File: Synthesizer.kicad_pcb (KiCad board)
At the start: 6 copper layers, 169 parts, among them J1 USB_A, J2 AudioJack3, J3 USB_B_Micro, J4 FPGA_debug, J5 MCU_debug, J6 67997-410HLF, SW1 SW_Push, SW10 SW_Push, SW11 SW_Push, SW12 SW_Push, SW13 SW_Push, SW14 SW_Push, SW15 SW_Push, SW16 SW_Push, SW2 SW_Push, SW3 SW_Push, SW4 SW_Push, SW5 SW_Push, SW6 SW_Push, SW7 SW_Push, SW8 SW_Push, SW9 SW_Push, U1 TPD3S014, U2 S25FL127S, U3 XC7A100T-FTG256, U4 Oscillator, U5 TPS54325, U6 TPS54294, U7 EFM32GG11B4xx, U8 PCM5102, Y1 48Mhz

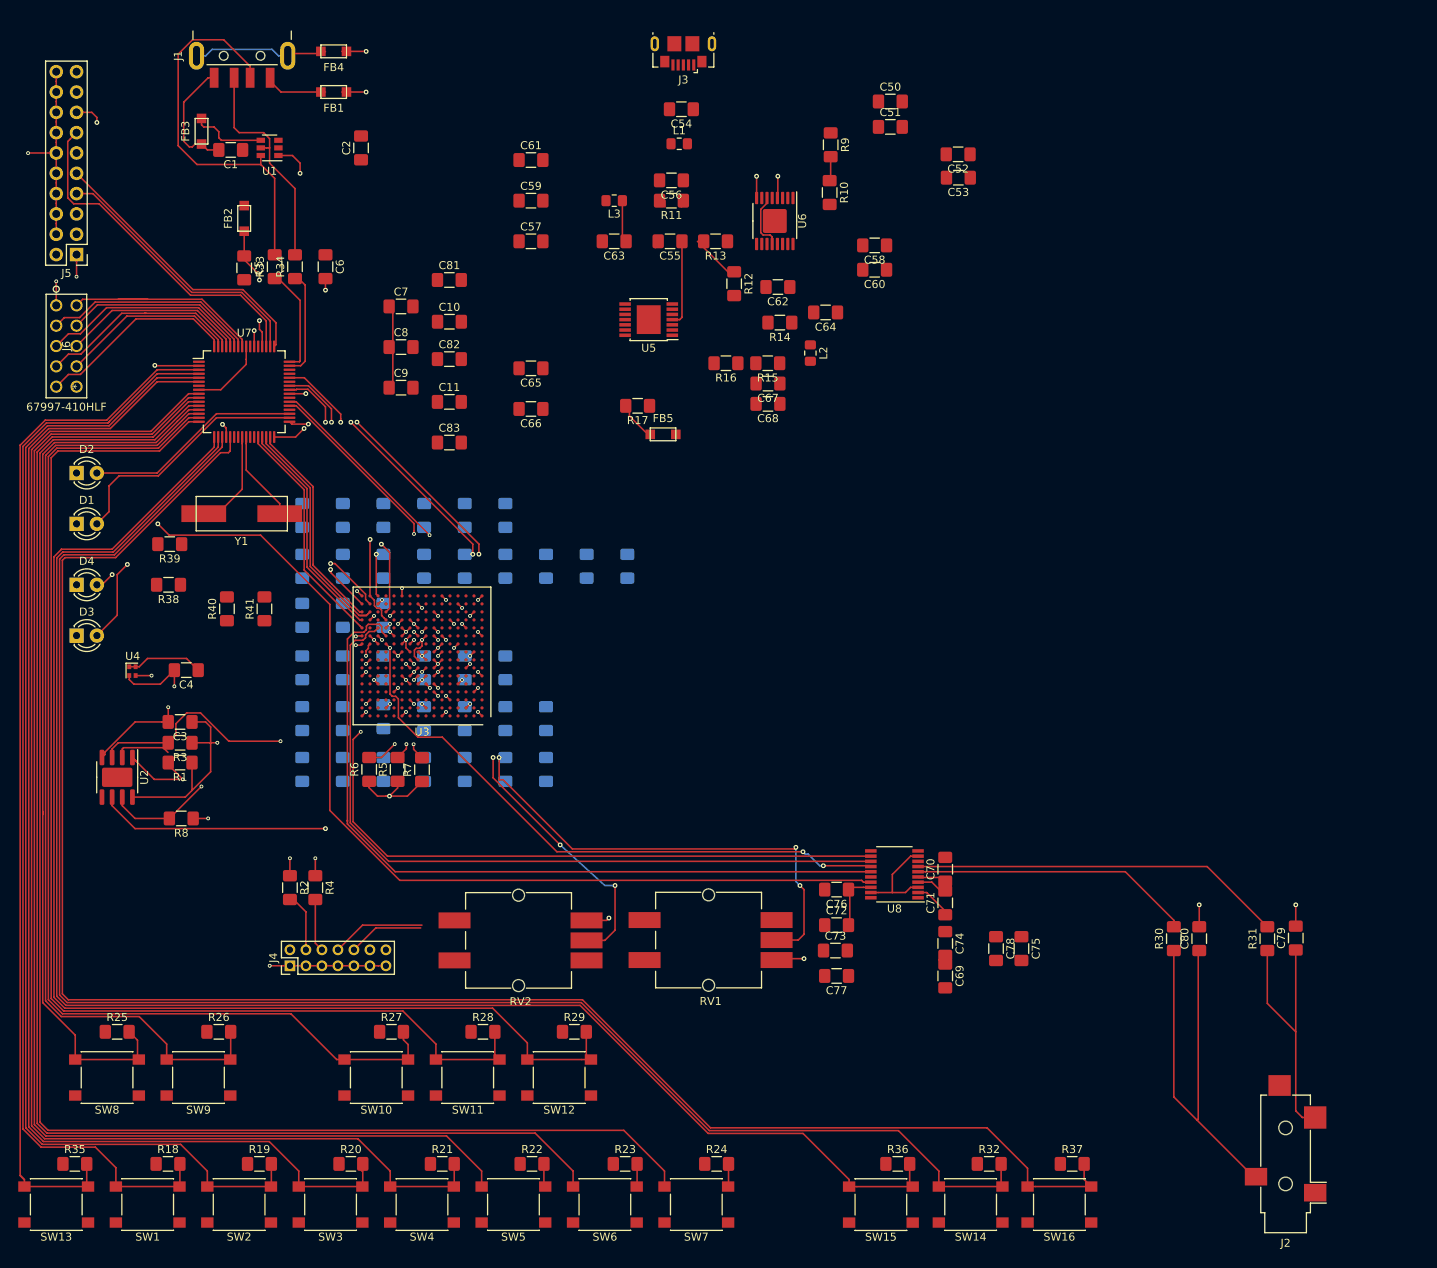
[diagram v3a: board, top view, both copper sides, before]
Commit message: Wire up 1V PSU. Use smaller footprints for small caps.
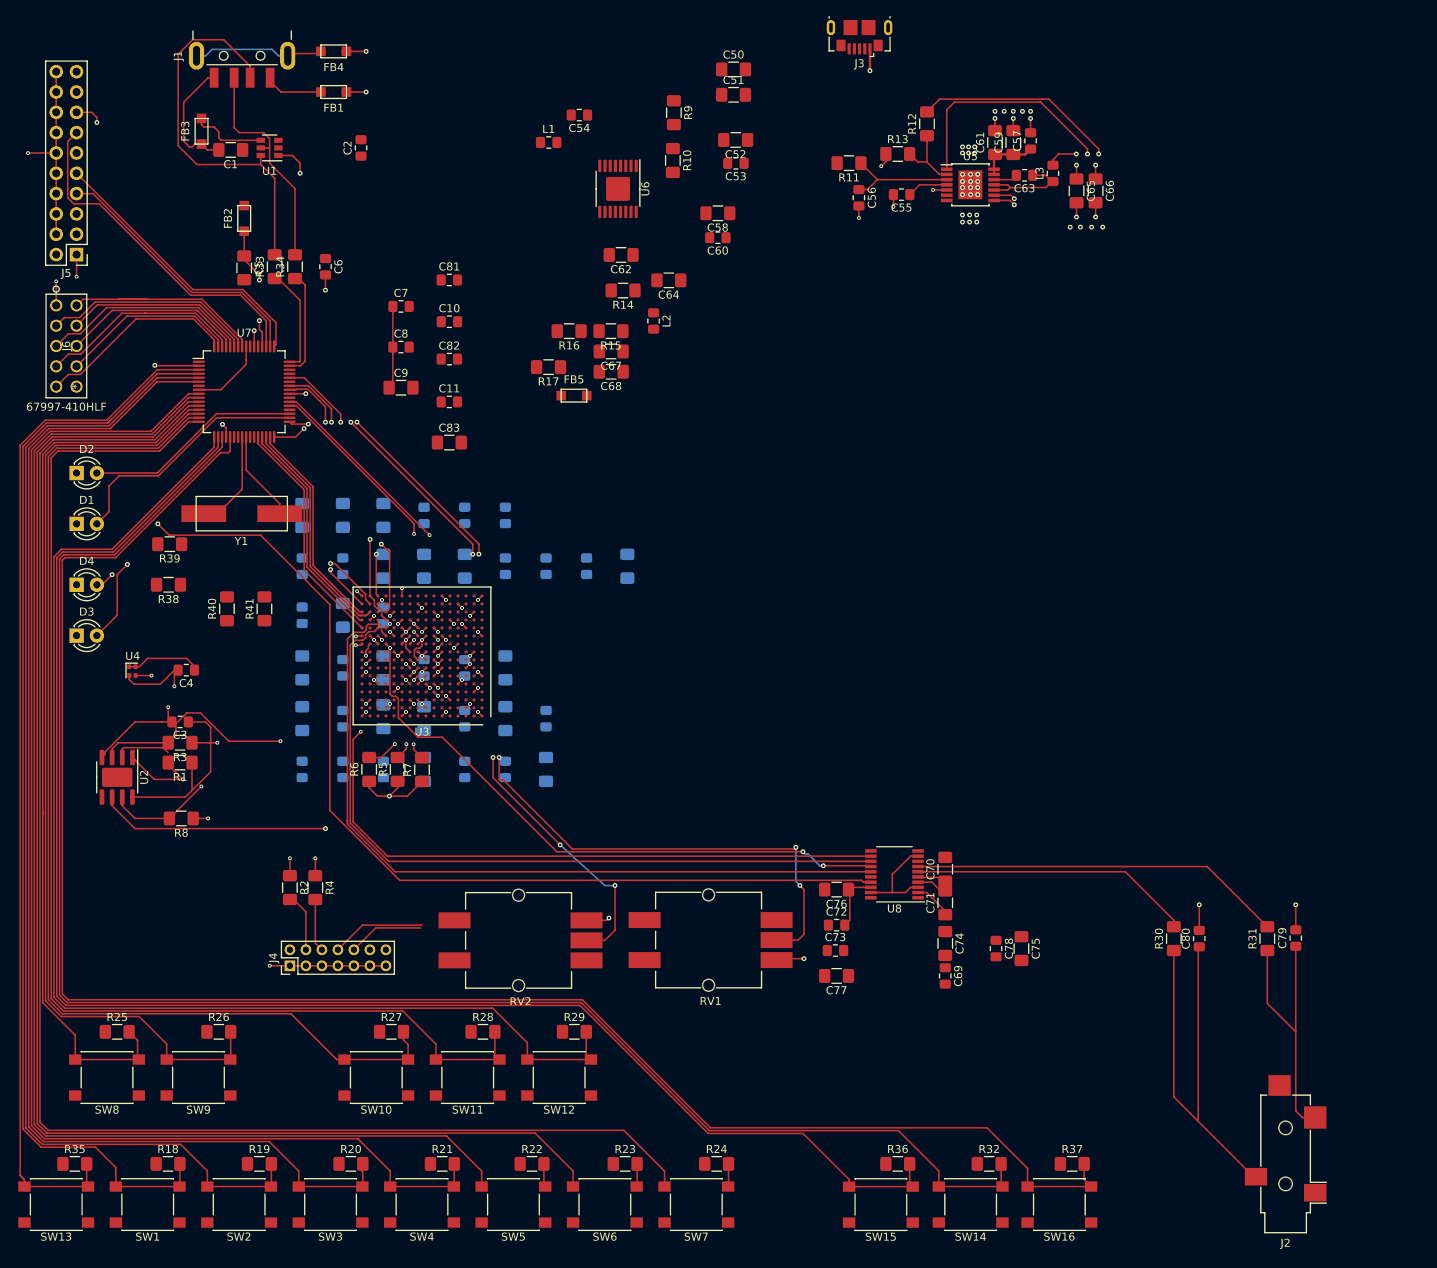
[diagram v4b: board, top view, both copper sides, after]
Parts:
- C10, C11, C18, C22, C23, C26, C29, C3, C30, C32, C34, C35, C36, C37, C38, C4, C40, C42, C43, C44, C45, C46, C47, C48, C49, C53, C55, C56, C57, C6, C60, C63, C7, C79, C8, C80, C81, C82: footprint Capacitor_SMD:C_1206_3216Metric_Pad1.42x1.75mm_HandSolder -> Capacitor_SMD:C_0805_2012Metric_Pad1.15x1.40mm_HandSolder
- C2, C54, C69, C72, C73, C78: value 0.1u -> 100n; footprint Capacitor_SMD:C_1206_3216Metric_Pad1.42x1.75mm_HandSolder -> Capacitor_SMD:C_0805_2012Metric_Pad1.15x1.40mm_HandSolder
- C64: value 0.1u -> 100n
- moved C66 75.7 mm to (147.7, 32.0), turned to 270 degrees
- moved C65 71.7 mm to (145.3, 32.0), turned to 270 degrees
- moved C57 63.7 mm to (139.6, 25.8), turned to 90 degrees
- moved C59 60.7 mm to (137.4, 26.0), turned to 90 degrees
- moved C61 58.0 mm to (135.1, 26.0), turned to 90 degrees
- moved L3 54.9 mm to (142.4, 29.9), turned to 90 degrees
- moved C63 52.0 mm to (138.8, 30.1)
- moved U5 43.6 mm to (132.1, 31.3), turned to 0 degrees
- moved R12 31.3 mm to (126.6, 23.7), turned to 90 degrees
- moved C55 29.5 mm to (123.5, 32.5)
- moved C52 27.9 mm to (102.7, 25.7)
- moved C53 27.9 mm to (102.7, 28.6)
- moved R13 25.3 mm to (123.0, 27.4), turned to 0 degrees
- moved C56 23.5 mm to (118.1, 32.9), turned to 270 degrees
- moved R11 22.7 mm to (116.9, 28.6)
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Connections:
- C75 pad 1: +3V3 -> +3.3VA
- C78 pad 1: +3V3 -> +3.3VA
- U8 pad 8: +3V3 -> +3.3VA
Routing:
- net +1V0: track 8.98 -> 70.1 mm, vias 5 -> 10
- net GND: track 136.7 -> 169.7 mm, vias 51 -> 93
- net Net-(C56-Pad1): track 1.49 -> 14.4 mm
- net +5V: track 0.00 -> 10.0 mm, vias 0 -> 1
- net Net-(C63-Pad1): track 5.08 -> 12.6 mm
- net Net-(R14-Pad2): track 7.18 -> 0.00 mm
- net Net-(C55-Pad1): track 10.8 -> 5.13 mm
- net Net-(FB5-Pad2): track 4.17 -> 0.00 mm
- net Net-(R10-Pad1): track 3.05 -> 0.00 mm
- net Net-(C63-Pad2): track 0.00 -> 3.02 mm
- net Net-(R12-Pad1): track 6.17 -> 8.98 mm
- net Net-(R11-Pad2): track 0.80 -> 0.00 mm
- added copper zone on PWR_plane, net +1V0
- added copper zone on GND_plane, net GND

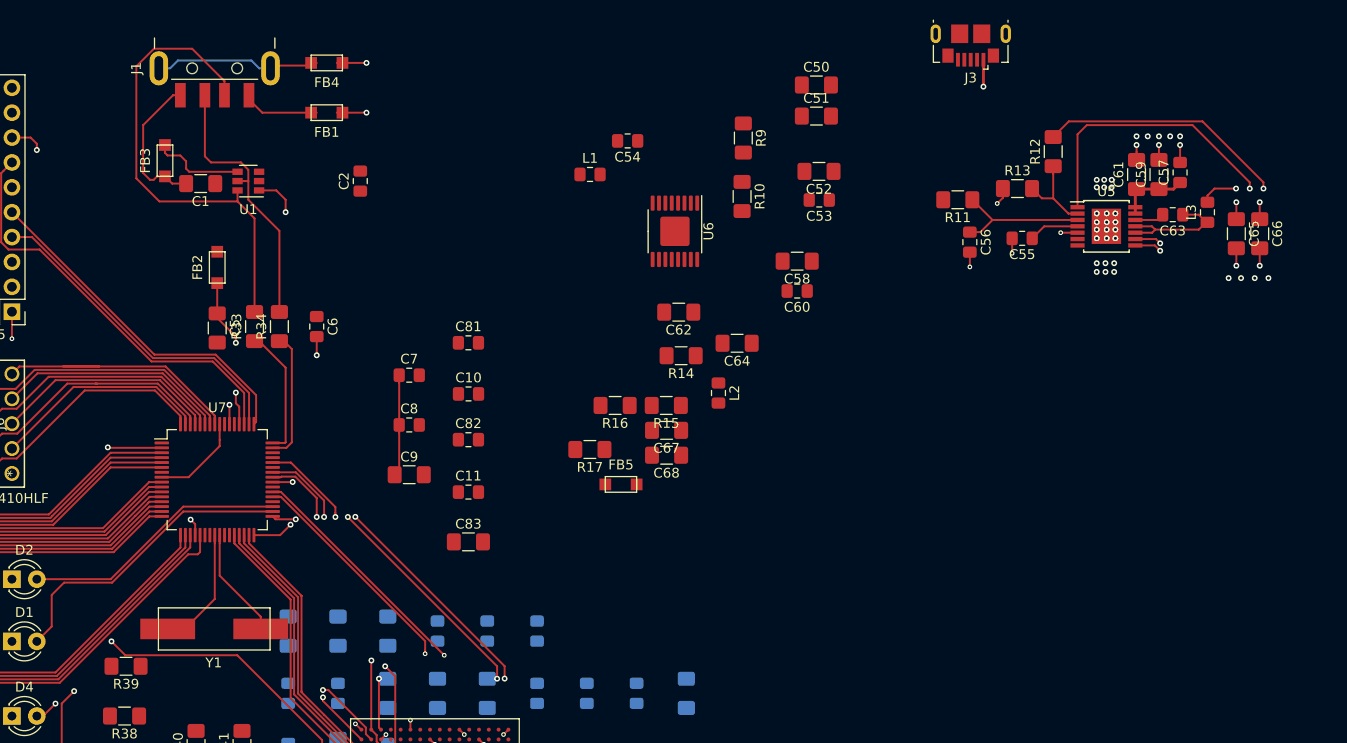
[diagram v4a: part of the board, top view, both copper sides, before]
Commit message: Wire up other PSU
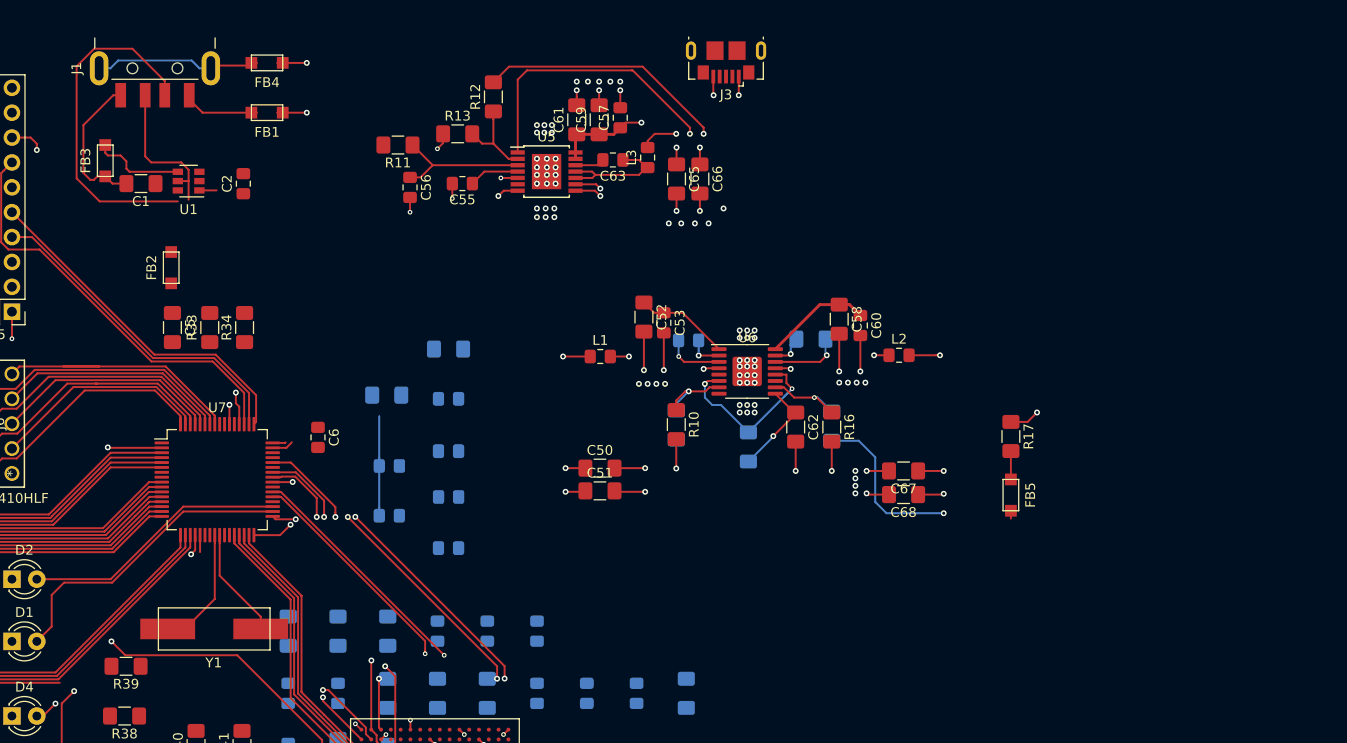
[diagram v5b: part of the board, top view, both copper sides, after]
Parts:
- C10, C11, C54, C64, C7, C8, C81, C82, C83, C9, R14, R15, R9: moved to B.Cu
- moved C55 57.4 mm to (66.3, 26.9)
- moved C57 57.4 mm to (82.4, 20.2)
- moved C65 57.4 mm to (88.2, 26.5)
- moved R12 57.4 mm to (69.5, 18.1)
- moved C56 57.4 mm to (61.0, 27.3)
- moved C59 57.4 mm to (80.3, 20.4)
- moved C61 57.4 mm to (78.0, 20.4)
- moved C63 57.4 mm to (81.7, 24.5)
- moved C66 57.4 mm to (90.6, 26.5)
- moved L3 57.4 mm to (85.2, 24.3)
- moved R11 57.4 mm to (59.7, 23.0)
- moved R13 57.4 mm to (65.8, 21.8)
- moved U5 57.4 mm to (74.9, 25.7)
- moved C50 44.9 mm to (80.3, 56.0)
- moved C51 44.2 mm to (80.3, 58.3)
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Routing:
- net +5V: track 10.0 -> 75.7 mm, vias 1 -> 3
- net GND: track 169.7 -> 213.4 mm, vias 93 -> 144
- net /EFM32/USB_VBUSEN: track 31.0 -> 3.73 mm, vias 2 -> 1
- net +3V3: track 71.7 -> 98.2 mm, vias 17 -> 21
- net /Button15: track 225.7 -> 205.8 mm
- net Net-(R14-Pad2): track 0.00 -> 19.0 mm, vias 0 -> 2
- net Net-(J1-Pad3): track 48.9 -> 35.3 mm
- net Net-(C64-Pad2): track 0.00 -> 13.6 mm, vias 0 -> 2
- net Net-(J1-Pad2): track 28.6 -> 15.4 mm
- net Net-(C54-Pad2): track 0.00 -> 13.0 mm, vias 0 -> 2
- net Net-(C6-Pad2): track 17.9 -> 5.52 mm, vias 2 -> 1
- net /EFM32/USB_D+: track 13.5 -> 1.35 mm
- net Net-(C5-Pad1): track 14.9 -> 3.37 mm, vias 2 -> 1
- net /EFM32/USB_D-: track 13.5 -> 2.19 mm
- net Net-(C62-Pad1): track 0.00 -> 9.88 mm, vias 0 -> 1
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- added copper zone on PWR_plane, net +1V8
- added copper zone on PWR_plane, net +3V3
